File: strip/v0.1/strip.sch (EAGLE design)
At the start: 102 parts, among them IC1 LP2992, IC2 ADP3110A-SO8, IC3 MAX3051, IC4 OPA335, IC5 ADP3110A-SO8, IC6 ADP3110A-SO8, IC7 STM32F050CX, Q1 IRF7828, Q2 IRF7828, Q3 IRF7828, Q4 IRF7828, Q5 IRF7828, Q6 IRF7828

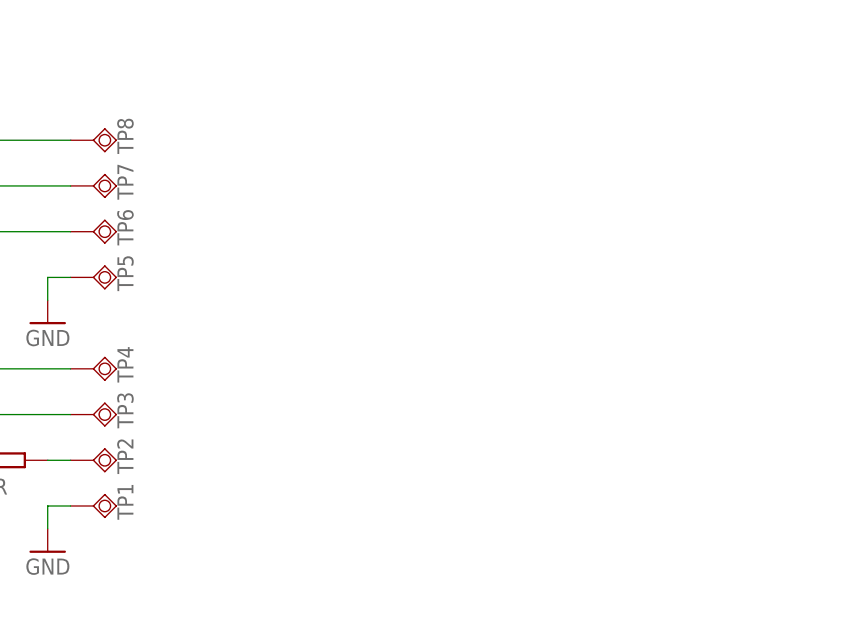
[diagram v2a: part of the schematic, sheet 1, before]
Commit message: Added some more documentation to the schematic.
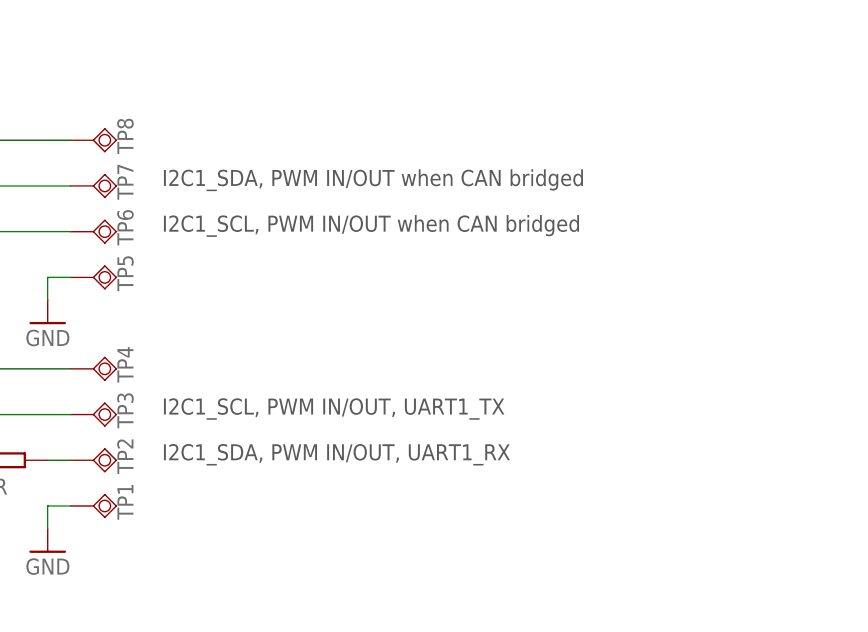
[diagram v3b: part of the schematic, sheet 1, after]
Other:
- note added: "I2C1_SCL, PWM IN/OUT when CAN bridged"
- note added: "I2C1_SCL, PWM IN/OUT, UART1_TX"
- note added: "I2C1_SDA, PWM IN/OUT when CAN bridged"
- note added: "I2C1_SDA, PWM IN/OUT, UART1_RX"
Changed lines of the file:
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@@
 <text x="226.06" y="93.98" size="1.778" layer="97">Alt: DNP=F</text>
 <text x="187.96" y="111.76" size="1.778" layer="97" rot="R90">Alt: DNP=F</text>
+<text x="127" y="53.34" size="1.778" layer="97">I2C1_SDA, PWM IN/OUT when CAN bridged</text>
+<text x="127" y="48.26" size="1.778" layer="97">I2C1_SCL, PWM IN/OUT when CAN bridged</text>
+<text x="127" y="27.94" size="1.778" layer="97">I2C1_SCL, PWM IN/OUT, UART1_TX</text>
+<text x="127" y="22.86" size="1.778" layer="97">I2C1_SDA, PWM IN/OUT, UART1_RX</text>
 </plain>
 <instances>

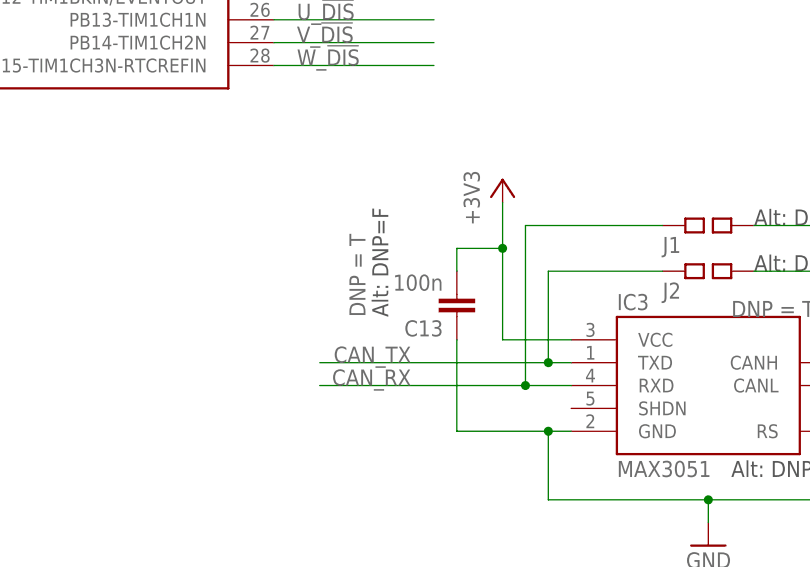
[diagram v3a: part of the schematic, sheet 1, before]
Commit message: Added more bom part number attributes.
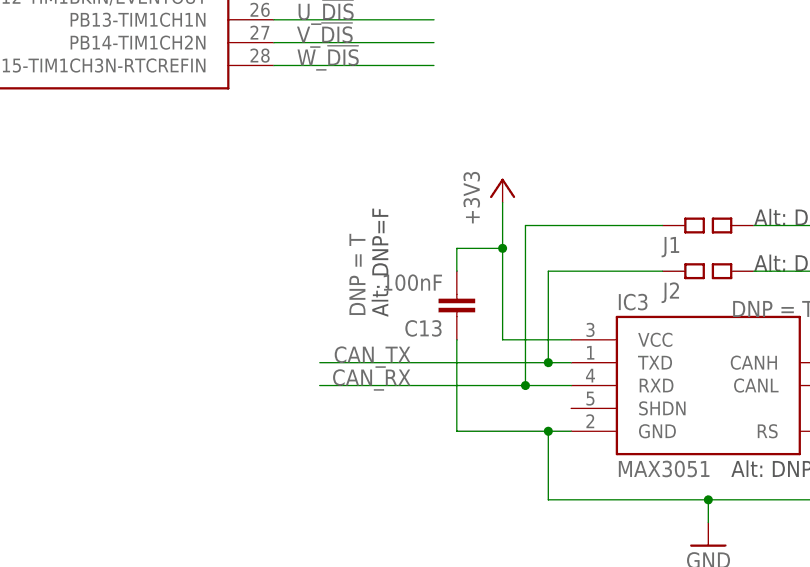
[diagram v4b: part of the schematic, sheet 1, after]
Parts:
- C13: value 100n -> 100nF
- D1, D3, D4: PARTNO * -> diode-sod-123
- IC3: PARTNO * -> ic-so8-can-3v3
- IC7: PARTNO mcu-tqfp-32-stm32f05 -> mcu-lqfp-48-stm32f05
- R15, R17, R22: PARTNO * -> res-0402-3k6
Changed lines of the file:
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@@
 <part name="FRAME2" library="frames" deviceset="A3L-LOC" device=""/>
 <part name="D1" library="pel_dipol_comp" deviceset="DIODE" device="-SOD-123" value="BAS21">
-<attribute name="PARTNO" value="*"/>
+<attribute name="PARTNO" value="diode-sod-123"/>
 </part>
 <part name="C23" library="pel_dipol_comp" deviceset="CAPACITOR" device="-0603" value="1u">
@@
 <part name="GND7" library="supply1" deviceset="GND" device=""/>
 <part name="D3" library="pel_dipol_comp" deviceset="DIODE" device="-SOD-123" value="BAS21">
-<attribute name="PARTNO" value="*"/>
+<attribute name="PARTNO" value="diode-sod-123"/>
 </part>
 <part name="C24" library="pel_dipol_comp" deviceset="CAPACITOR" device="-0603" value="1u">
@@
 </part>
 <part name="D4" library="pel_dipol_comp" deviceset="DIODE" device="-SOD-123" value="BAS21">
-<attribute name="PARTNO" value="*"/>
+<attribute name="PARTNO" value="diode-sod-123"/>
 </part>
 <part name="C25" library="pel_dipol_comp" deviceset="CAPACITOR" device="-0603" value="1u">
@@
 </part>
 <part name="R15" library="pel_dipol_comp" deviceset="RESISTOR" device="-0402" value="3k6">
-<attribute name="PARTNO" value="*"/>
+<attribute name="PARTNO" value="res-0402-3k6"/>
 </part>
 <part name="R16" library="pel_dipol_comp" deviceset="RESISTOR" device="-0402" value="10k">
@@
 </part>
 <part name="R17" library="pel_dipol_comp" deviceset="RESISTOR" device="-0402" value="3k6">
-<attribute name="PARTNO" value="*"/>
+<attribute name="PARTNO" value="res-0402-3k6"/>
 </part>
 <part name="R18" library="pel_dipol_comp" deviceset="RESISTOR" device="-0402" value="10k">
@@
 </part>
 <part name="R22" library="pel_dipol_comp" deviceset="RESISTOR" device="-0402" value="3k6">
-<attribute name="PARTNO" value="*"/>
+<attribute name="PARTNO" value="res-0402-3k6"/>
 </part>
 <part name="C26" library="pel_dipol_comp" deviceset="CAPACITOR" device="-0402" value="100nF">
@@
 <part name="P+2" library="supply1" deviceset="+3V3" device=""/>
 <part name="IC7" library="pel_stm32" deviceset="STM32F050CX" device="">
-<attribute name="PARTNO" value="mcu-tqfp-32-stm32f05"/>
+<attribute name="PARTNO" value="mcu-lqfp-48-stm32f05"/>
 </part>
 <part name="C5" library="pel_dipol_comp" deviceset="CAPACITOR-POL" device="D" value="220uF">
@@
 <attribute name="PARTNO" value="*"/>
 </part>
-<part name="C13" library="pel_dipol_comp" deviceset="CAPACITOR" device="-0402" value="100n">
+<part name="C13" library="pel_dipol_comp" deviceset="CAPACITOR" device="-0402" value="100nF">
 <attribute name="DNP" value="T"/>
 <attribute name="PARTNO" value="cap-cer-0402-100n"/>
@@
 <part name="IC3" library="open-bldc" deviceset="MAX3051" device="">
 <attribute name="DNP" value="T"/>
-<attribute name="PARTNO" value="*"/>
+<attribute name="PARTNO" value="ic-so8-can-3v3"/>
 </part>
 <part name="GND4" library="supply1" deviceset="GND" device=""/>
